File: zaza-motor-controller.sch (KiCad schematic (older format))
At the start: 74 parts, among them J1 VIN, J2 VIN, J3 CONN_02X05, J4 CONN_02X01, J5 GS3, Q1 3904, Q10 3906, Q11 3904, Q12 3904, Q2 3904, Q3 3906, Q4 3904, Q5 IXTA220, Q6 IXTA220, Q7 IXTA220, Q8 IXTA220, Q9 3904, U1 74HC00, U2 74HC00, U3 LM358, U4 LM555N

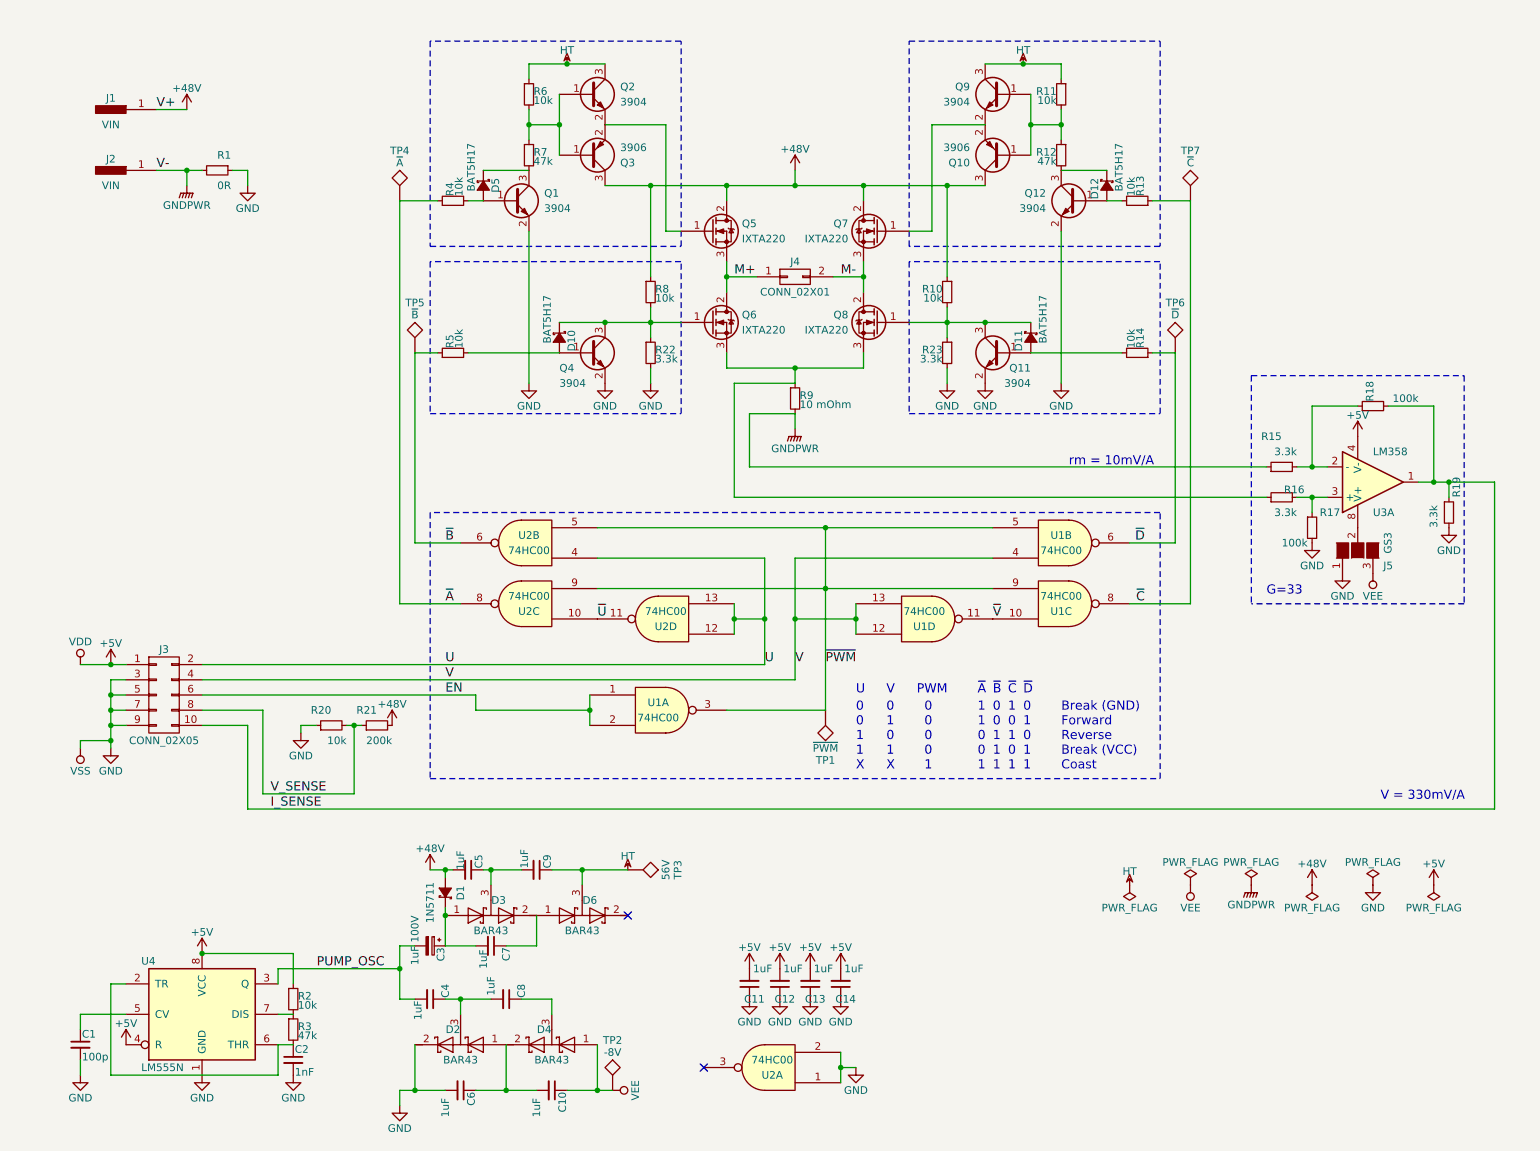
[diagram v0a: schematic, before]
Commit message: Add Rev 1 schematic
We've changed the FET driving circuit to use IRS2003 drivers instead
of discrete logic. There is also an ADC and a SPI bus with encoded
chip-select.
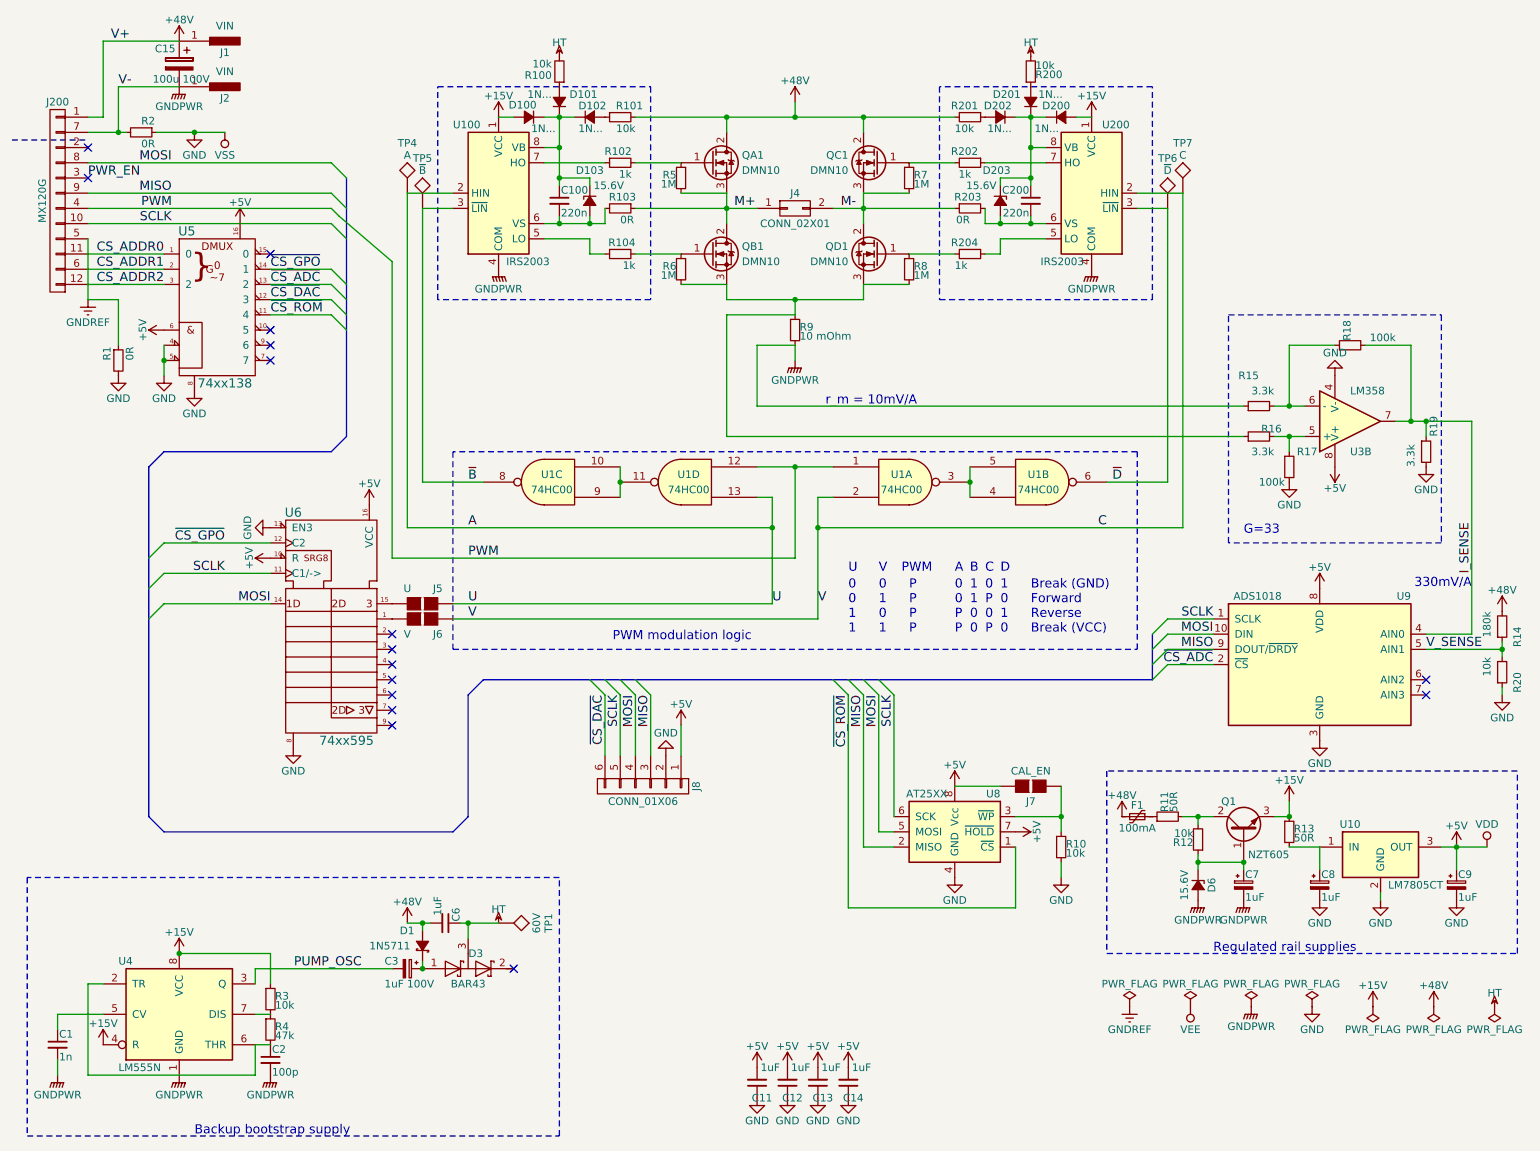
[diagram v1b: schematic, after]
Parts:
- removed C10, C4, C5, C7, C8, C9: 1uF, Capacitors_SMD:C_0805, symbol C_Small
- removed D10, D11, D12, D5: BAT5H17, Diodes_SMD:D_MiniMELF_Standard, symbol D_Schottky_Small_ALT
- removed D2, D4, D6: BAR43, TO_SOT_Packages_SMD:SOT-23, symbol D_Schottky_x2_Serial_AKC
- removed J3: CONN_02X05, Connectors:IDC_Header_Straight_10pins, symbol CONN_02X05
- removed J5: GS3, Connectors:GS3, symbol GS3
- removed Q1, Q11, Q12, Q2, Q4, Q9: 3904, TO_SOT_Packages_SMD:SOT-23, symbol Q_NPN_BEC
- removed Q10, Q3: 3906, TO_SOT_Packages_SMD:SOT-23, symbol Q_PNP_BEC
- removed R21: 200k, Resistors_SMD:R_0805, symbol R_Small
- removed R22, R23: 3.3k, Resistors_SMD:R_0805, symbol R_Small
- removed TP2: -8V, Measurement_Points:Test_Point_Keystone_5000-5004_Miniature, symbol TEST
- removed TP3: 56V, Measurement_Points:Test_Point_Keystone_5000-5004_Miniature, symbol TEST
- removed unit 4 of U1
- removed unit 1 of U1
- removed unit 3 of U2
- removed unit 4 of U2
- removed unit 1 of U2
- added C100, C200: 220n, Capacitors_SMD:C_0805, symbol C_Small
- added C15: 100u 100V, Capacitors_THT:CP_Axial_L29.0mm_D16.0mm_P35.00mm_Horizontal, symbol CP
- added C7, C8, C9: 1uF, Capacitors_SMD:C_0805, symbol CP_Small
- added D100, D101, D102, D200, D201, D202: 1N..., Diodes_SMD:D_MiniMELF_Standard, symbol D_Small_ALT
- added D103, D203, D6: 15.6V, Diodes_SMD:D_SMA_Standard, symbol D_Zener_Small_ALT
- added F1: 100mA, Resistors_SMD:R_1206, symbol Polyfuse_Small
- added J200: MX120G, molex-120g:Molex_MX120G_02x06_3.5mm_36783-1201, symbol MX120G
- added J5: U, Pin_Headers:Pin_Header_Straight_2x01_Pitch2.54mm, symbol GS2
- added J6: V, Pin_Headers:Pin_Header_Straight_2x01_Pitch2.54mm, symbol GS2
- added J7: CAL_EN, Pin_Headers:Pin_Header_Straight_2x01_Pitch2.54mm, symbol GS2
- added J8: CONN_01X06, Pin_Headers:Pin_Header_Straight_1x06_Pitch2.54mm, symbol CONN_01X06
- added Q1: NZT605, TO_SOT_Packages_SMD:SOT-223-3Lead_TabPin2, symbol Q_NPN_BCE
- added R100, R101, R200, R201: 10k, Resistors_SMD:R_0805, symbol R_Small
- added R102, R104, R202, R204: 1k, Resistors_SMD:R_0805, symbol R_Small
- added R103, R203: 0R, Resistors_SMD:R_0805, symbol R_Small
- added unit 2 of U1
- added U10: LM7805CT, TO_SOT_Packages_SMD:SOT-223-3Lead_TabPin2, symbol LM7805CT
- added U100, U200: IRS2003, Housings_SOIC:SOIC-8_3.9x4.9mm_Pitch1.27mm, symbol IRS2003
- added U5: 74xx138, Housings_SOIC:SOIC-16_3.9x9.9mm_Pitch1.27mm, symbol 74xx138
- added U6: 74xx595, Housings_SOIC:SOIC-16_3.9x9.9mm_Pitch1.27mm, symbol 74xx595
- added U8: AT25XX, Housings_SOIC:SOIC-8_3.9x4.9mm_Pitch1.27mm, symbol AT25_EEPROM
- added U9: ADS1018, Housings_SSOP:MSOP-10_3x3mm_Pitch0.5mm, symbol ADS1118I
- C1: value 100p -> 1n
- C2: value 1nF -> 100p
- D1: footprint Diodes_THT:D_DO-35_SOD27_P7.62mm_Horizontal -> Diodes_SMD:D_MiniMELF_Standard
- QA1: renamed from Q5; value IXTA220 -> DMN10; footprint TO_SOT_Packages_SMD:SOT-404 -> TO-SMD:SOT-404-thermal-vias
- QB1: renamed from Q6; value IXTA220 -> DMN10; footprint TO_SOT_Packages_SMD:SOT-404 -> TO-SMD:SOT-404-thermal-vias
- QC1: renamed from Q7; value IXTA220 -> DMN10; footprint TO_SOT_Packages_SMD:SOT-404 -> TO-SMD:SOT-404-thermal-vias
- QD1: renamed from Q8; value IXTA220 -> DMN10; footprint TO_SOT_Packages_SMD:SOT-404 -> TO-SMD:SOT-404-thermal-vias
- R11, R13: value 10k -> 50R; footprint Resistors_SMD:R_0805 -> Resistors_SMD:R_2010
- R12, R3: value 47k -> 10k
- R14: value 10k -> 180k
- R2: value 10k -> 0R
- R4: value 10k -> 47k
- R5, R6, R8: value 10k -> 1M
- R7: value 47k -> 1M
- TP1: value ~PWM -> 60V
- TP4: value ~A -> A
- TP7: value ~C -> C
- renumbered U2 to U1
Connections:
- net +48V: now also C6.2, R14.2, C15.1, F1.2, J200.1 (P1), R101.2, R201.2; no longer R10.1, R8.1
- net +5V: now also U3.8 (V+), C9.1, J7.1 (G1), J8.1 (P1), U1.14 (VDD), U10.3 (OUT), U5.16, U5.6, U6.10 (R), U6.16 (VCC), U8.7 (~HOLD), U8.8 (Vcc), U9.8 (VDD); no longer R2.1, U3.4 (V-), U4.4 (R), U4.8 (VCC)
- net GND: now also R1.2, R10.2, R2.1, U3.4 (V-), C8.2, C9.2, J8.2 (P2), U1.7 (VSS), U10.2 (GND), U5.4, U5.5, U5.8, U6.13 (EN3), U6.8, U8.4 (GND), U9.3 (GND); no longer C1.2, C2.2, C6.2, R1.1, U4.1 (GND)
- net GNDPWR: now also C1.2, C2.2, R2.2, U4.1 (GND), C15.2, C7.2, D6.2 (A), J200.7 (P7), U100.4 (COM), U200.4 (COM); no longer R1.2
- net HT: now also C6.1, D3.3 (common), TP1.1, R100.2, R200.2; no longer R11.1, R6.1
- net I_SENSE: now also U3.7, U9.4 (AIN0); no longer U3.1
- net M+: now also R5.2, R103.1
- net M-: now also R7.2, R203.1
- net V_SENSE: now also R14.1, U9.5 (AIN1)
- net ~B: now also U1.8, U100.3 (~LIN); no longer R5.1, U1.6
- net ~D: now also U1.6, U200.3 (~LIN); no longer R14.1, U1.6
- net at QA1.1 (G): now also R5.1, R102.2
- net at QB1.1 (G): now also R6.1, R104.2; no longer R8.2
- net at QB1.3 (S), QD1.3 (S), R16.1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: now also R6.2, R8.2
- net at QC1.1 (G): now also R7.1, R202.2
- net at QD1.1 (G): now also R8.1, R204.2; no longer R10.2
- net at C2.1, U4.2 (TR), U4.6 (THR): now also R4.2; no longer R3.2
- net at R15.2, R18.1: now also U3.6 (-); no longer U3.2 (-)
- net at R16.2, R17.1: now also U3.5 (+); no longer U3.3 (+)
- net at R12.2: now also R11.2, Q1.2 (C)
- net at R13.2: now also C8.1, U10.1 (IN)
- net at R12.1: now also C7.1, D6.1 (K), Q1.1 (B); no longer R11.2
- removed net U: U1.4
- removed net V: U1.4
- net ~A: no longer names the net of R4.1
- net ~A: now also R3.2, U4.7 (DIS); no longer TP4.1
- removed net ~C: R13.1, TP7.1, U1.8
- removed net ~PWM: TP1.1, U1.5, U1.5, U1.9
- net ~V: no longer names the net of U1.10
- net ~V: now also U1.11, U1.9
- new net: U1.3, U1.4, U1.5
- new net: J6.2 (G2), U6.1
- new net: J5.2 (G2), U6.15
- new net: F1.1, R11.1
- new net: R104.1, U100.5 (LO)
- new net: C100.2, D103.2 (A), R103.2, U100.6 (VS)
- new net: R102.1, U100.7 (HO)
- new net: C100.1, D100.1 (K), D101.1 (K), D102.1 (K), D103.1 (K), U100.8 (VB)
- new net: D102.2 (A), R101.1
- new net: D101.2 (A), R100.1
- new net: R204.1, U200.5 (LO)
- new net: C200.2, D203.2 (A), R203.2, U200.6 (VS)
- new net: R202.1, U200.7 (HO)
- new net: C200.1, D200.1 (K), D201.1 (K), D202.1 (K), D203.1 (K), U200.8 (VB)
- new net: D202.2 (A), R201.1
- new net: D201.2 (A), R200.1
- new net: J7.2 (G2), R10.1, U8.3 (~WP)
- new net +15V: D100.2 (A), D200.2 (A), Q1.3 (E), R13.1, R3.1, U100.1 (VCC), U200.1 (VCC), U4.4 (R), U4.8 (VCC)
- new net A: J5.1 (G1), TP4.1, U1.13, U100.2 (HIN)
- new net C: J6.1 (G1), TP7.1, U1.2, U200.2 (HIN)
- new net CS_ADDR0: J200.11 (P11), U5.1 (0)
- new net CS_ADDR1: J200.6 (P6), U5.2
- new net CS_ADDR2: J200.12 (P12), U5.3 (2)
- new net GNDREF: J200.5 (P5), R1.1
- new net MISO: J200.9 (P9), J8.3 (P3), U8.2 (MISO), U9.9 (DOUT/~DRDY)
- new net MOSI: J200.8 (P8), J8.4 (P4), U6.14, U8.5 (MOSI), U9.10 (DIN)
- new net PWM: J200.4 (P4), U1.1, U1.12
- new net PWR_EN: J200.3 (P3)
- new net SCLK: J200.10 (P10), J8.5 (P5), U6.11 (C1/->), U8.6 (SCK), U9.1 (SCLK)
- new net ~CS_ADC: U5.13 (2), U9.2 (~CS)
- new net ~CS_DAC: J8.6 (P6), U5.12 (3)
- new net ~CS_GPO: U5.14 (1), U6.12 (C2)
- new net ~CS_ROM: U5.11 (4), U8.1 (~CS)
- no-connect marks 2 -> 16
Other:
- note added: "0\n0\n1\n1"
- note added: "0\n0\nP\nP"
- note added: "0\n1\n0\n1"
- note added: "0\nP\n0\nP"
- note added: "1\n0\n1\n0"
- note added: "1\n1\n0\n0"
- note added: "330mV/A"
- note added: "A"
- note added: "B"
- note added: "Backup bootstrap supply"
- note added: "Break (GND)\nForward\nReverse\nBreak (VCC)"
- note added: "C"
- note added: "D"
- note added: "PWM modulation logic"
- note added: "P\nP\nP\nP\n"
- note added: "Regulated rail supplies"
- note added: "r_m = 10mV/A"
- note removed: "0\n0\n0\n0\n1"
- note removed: "0\n0\n1\n1\n1"
- note removed: "0\n0\n1\n1\nX"
- note removed: "0\n1\n0\n1\n1"
- note removed: "0\n1\n0\n1\nX"
- note removed: "1\n0\n1\n0\n1"
- note removed: "1\n1\n0\n0\n1"
- note removed: "Break (GND)\nForward\nReverse\nBreak (VCC)\nCoast"
- note removed: "V = 330mV/A"
- note removed: "rm = 10mV/A"
- note removed: "~A"
- note removed: "~B"
- note removed: "~C"
- note removed: "~D"
- moved on the sheet: C11, C12, C13, C14, J1, J2, J4, QA1, QB1, QC1, QD1, R15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
